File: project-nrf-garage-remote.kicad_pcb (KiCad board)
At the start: 2 copper layers, 9 parts, among them J1 Screw_Terminal_01x02, J2 Screw_Terminal_01x04, Q1 BSS138W, Q2 BSS138W

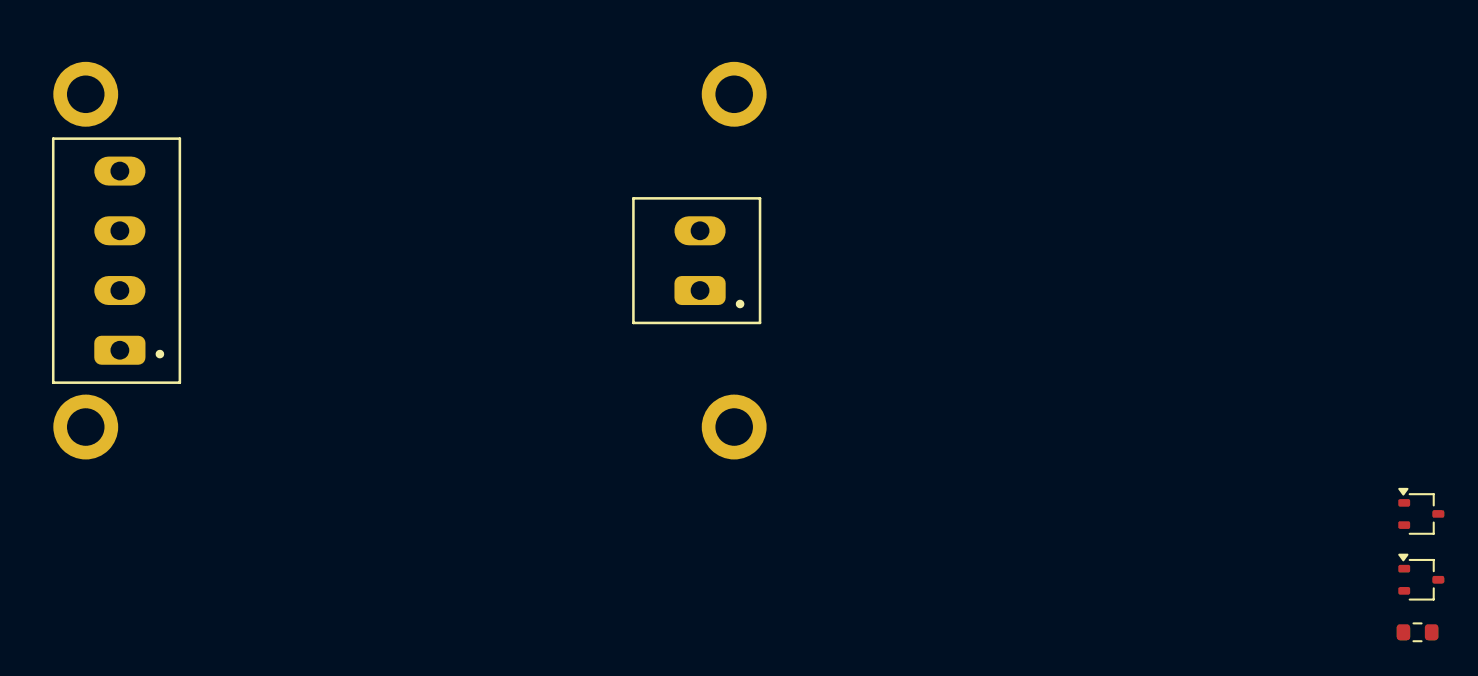
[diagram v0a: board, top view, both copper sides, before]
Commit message: Change the terminals footprint
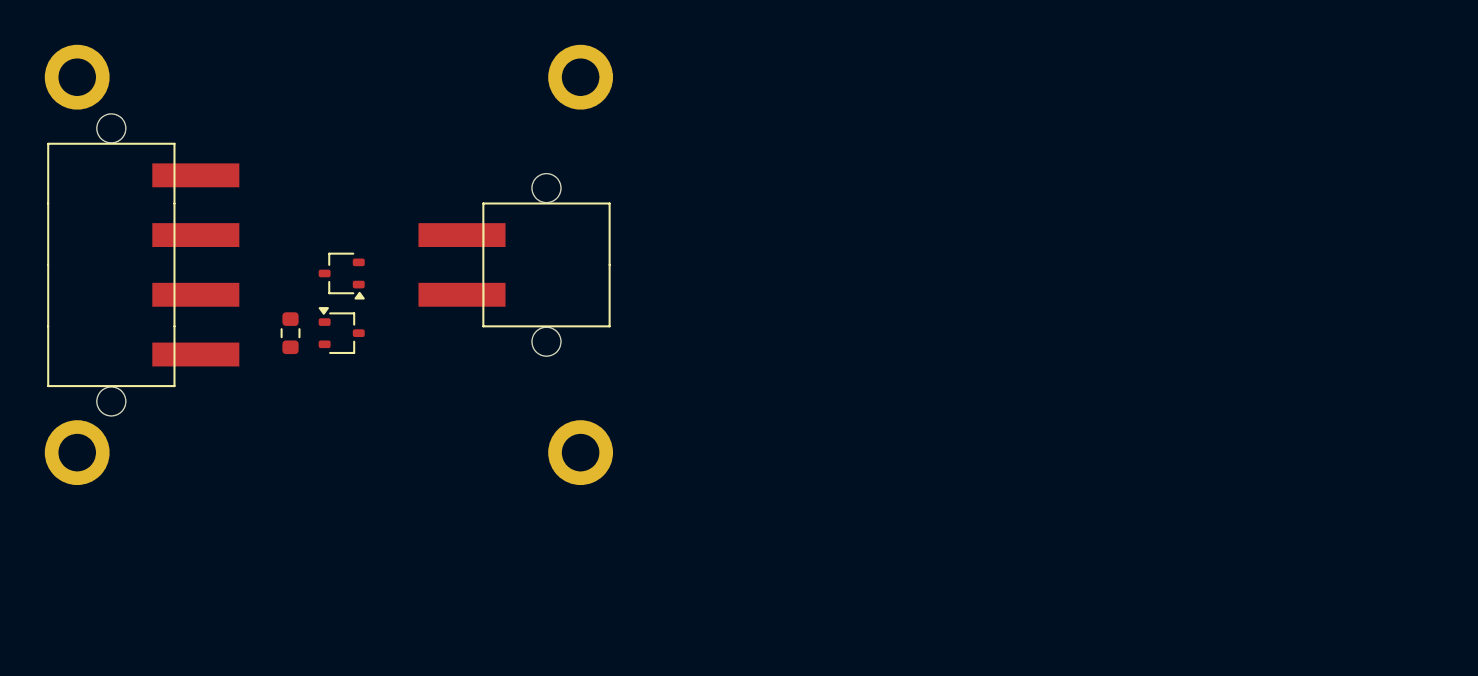
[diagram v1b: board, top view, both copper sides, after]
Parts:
- J1: footprint Conn_Molex_393570002:Molex-393570002-MFG -> TZ022101B000G:TZ022101B000G
- J2: footprint Conn_Molex_393570004:Molex-393570004-MFG -> TZ042101B000G:TZ042101B000G
- moved R1 68.3 mm to (36.0, 32.0), turned to -90 degrees
- moved Q2 65.8 mm to (39.0, 28.5), turned to 180 degrees
- moved Q1 64.1 mm to (39.0, 32.0)
- moved H4 9.12 mm to (53.0, 39.0)
- moved H3 9.06 mm to (53.0, 17.0)
- moved J1 8.81 mm to (51.0, 28.0)
- moved H2 1.58 mm to (23.5, 39.0)
- moved H1 1.12 mm to (23.5, 17.0)
- moved J2 0.39 mm to (25.5, 28.0), turned to -90 degrees

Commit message: Place parts
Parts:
- moved R1 9.34 mm to (38.5, 23.0), turned to 0 degrees
- moved Q1 6.52 mm to (38.5, 25.5)
- moved Q2 1.58 mm to (38.5, 30.0)
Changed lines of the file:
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@@
 	(footprint "BSS138W:BSS138W"
 		(layer "F.Cu")
-		(at 39 32)
+		(at 38.5 25.5)
 		(descr "SOT-323, SC-70")
 		(tags "SOT-323 SC-70")
@@
 	(footprint "BSS138W:BSS138W"
 		(layer "F.Cu")
-		(at 39 28.5 180)
+		(at 38.5 30 180)
 		(descr "SOT-323, SC-70")
 		(tags "SOT-323 SC-70")
@@
 	(footprint "Resistor_SMD:R_0603_1608Metric"
 		(layer "F.Cu")
-		(at 36 32 -90)
+		(at 38.5 23)
 		(descr "Resistor SMD 0603 (1608 Metric), square (rectangular) end terminal, IPC_7351 nominal, (Body size source: IPC-SM-782 page 72, https://www.pcb-3d.com/wordpress/wp-content/uploads/ipc-sm-782a_amendment_1_and_2.pdf), generated with kicad-footprint-generator")
 		(tags "resistor")
 		(property "Reference" "R1"
-			(at 0 -1.43 90)
+			(at 0 -1.43 360)
 			(layer "F.SilkS")
 			(hide yes)
@@
 		)
 		(property "Value" "PD"
-			(at 0 1.43 90)
+			(at 0 1.43 360)
 			(layer "F.Fab")
 			(hide yes)
@@
 		)
 		(property "Footprint" "Resistor_SMD:R_0603_1608Metric"
-			(at 0 0 -90)
+			(at 0 0 0)
 			(unlocked yes)
 			(layer "F.Fab")
@@
 		)
 		(property "Datasheet" ""
-			(at 0 0 -90)
+			(at 0 0 0)
 			(unlocked yes)
 			(layer "F.Fab")
@@
 		)
 		(property "Description" "Resistor"
-			(at 0 0 -90)
+			(at 0 0 0)
 			(unlocked yes)
 			(layer "F.Fab")
@@
 		(attr smd)
 		(fp_line
+			(start -0.237258 -0.5225)
+			(end 0.237258 -0.5225)
+			(stroke
+				(width 0.12)
+				(type solid)
+			)
+			(layer "F.SilkS")
+		)
+		(fp_line
 			(start -0.237258 0.5225)
 			(end 0.237258 0.5225)
@@
 		)
 		(fp_line
-			(start -0.237258 -0.5225)
-			(end 0.237258 -0.5225)
-			(stroke
-				(width 0.12)
-				(type solid)
-			)
-			(layer "F.SilkS")
+			(start -1.48 -0.73)
+			(end 1.48 -0.73)
+			(stroke
+				(width 0.05)
+				(type solid)
+			)
+			(layer "F.CrtYd")
 		)
 		(fp_line
@@
 		)
 		(fp_line
+			(start 1.48 -0.73)
+			(end 1.48 0.73)
+			(stroke
+				(width 0.05)
+				(type solid)
+			)
+			(layer "F.CrtYd")
+		)
+		(fp_line
 			(start 1.48 0.73)
 			(end -1.48 0.73)
@@
 		)
 		(fp_line
-			(start -1.48 -0.73)
-			(end 1.48 -0.73)
-			(stroke
-				(width 0.05)
-				(type solid)
-			)
-			(layer "F.CrtYd")
-		)
-		(fp_line
-			(start 1.48 -0.73)
-			(end 1.48 0.73)
-			(stroke
-				(width 0.05)
-				(type solid)
-			)
-			(layer "F.CrtYd")
+			(start -0.8 -0.4125)
+			(end 0.8 -0.4125)
+			(stroke
+				(width 0.1)
+				(type solid)
+			)
+			(layer "F.Fab")
 		)
 		(fp_line
@@
 		)
 		(fp_line
+			(start 0.8 -0.4125)
+			(end 0.8 0.4125)
+			(stroke
+				(width 0.1)
+				(type solid)
+			)
+			(layer "F.Fab")
+		)
+		(fp_line
 			(start 0.8 0.4125)
 			(end -0.8 0.4125)
@@
 			(layer "F.Fab")
 		)
-		(fp_line
-			(start -0.8 -0.4125)
-			(end 0.8 -0.4125)
-			(stroke
-				(width 0.1)
-				(type solid)
-			)
-			(layer "F.Fab")
-		)
-		(fp_line
-			(start 0.8 -0.4125)
-			(end 0.8 0.4125)
-			(stroke
-				(width 0.1)
-				(type solid)
-			)
-			(layer "F.Fab")
-		)
 		(fp_text user "${REFERENCE}"
-			(at 0 0 90)
+			(at 0 0 360)
 			(layer "F.Fab")
 			(effects
@@
 		)
 		(pad "1" smd roundrect
-			(at -0.825 0 270)
+			(at -0.825 0)
 			(size 0.8 0.95)
 			(layers "F.Cu" "F.Paste" "F.Mask")
@@
 		)
 		(pad "2" smd roundrect
-			(at 0.825 0 270)
+			(at 0.825 0)
 			(size 0.8 0.95)
 			(layers "F.Cu" "F.Paste" "F.Mask")

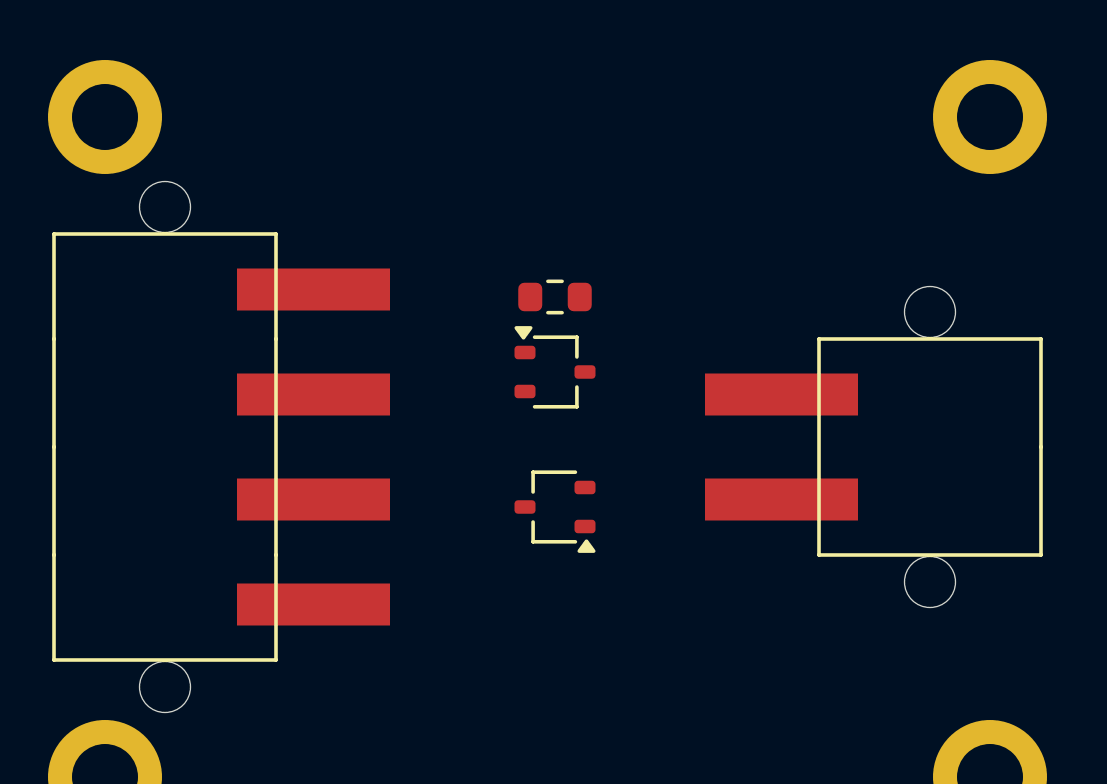
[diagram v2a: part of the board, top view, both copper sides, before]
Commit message: Add silkscreen
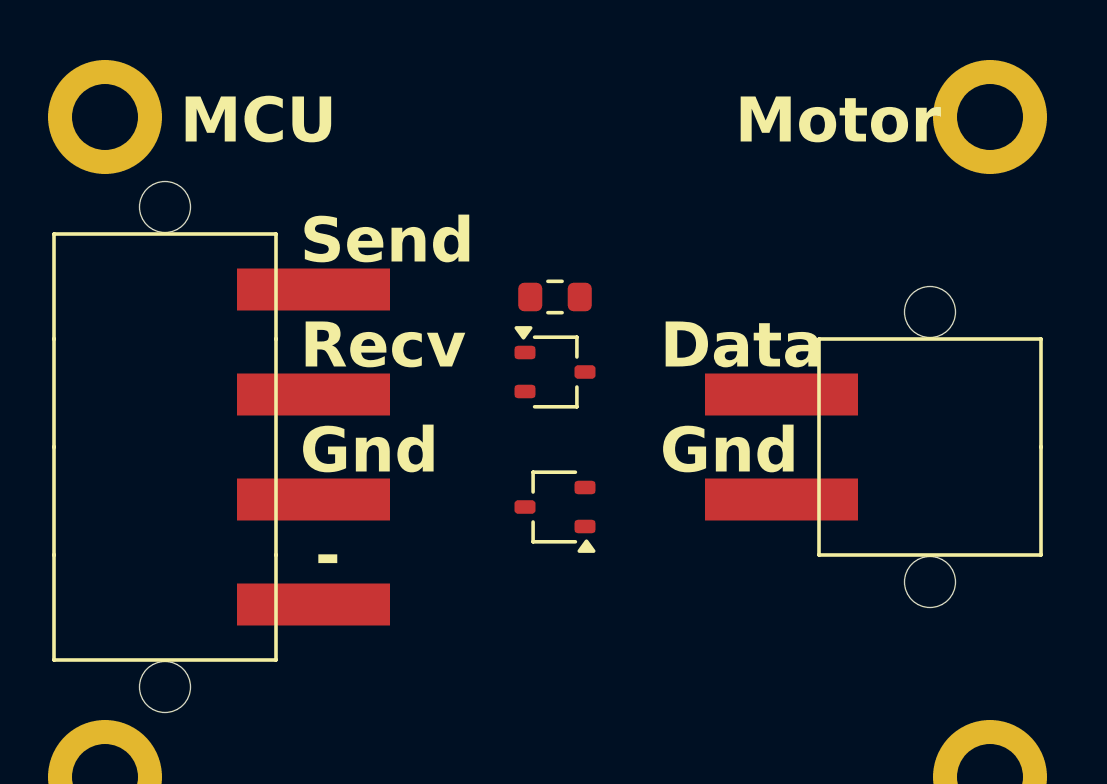
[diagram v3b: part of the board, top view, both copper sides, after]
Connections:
- J1 pad 1: /motor_data -> GND
- J1 pad 2: GND -> /motor_data
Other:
- board text added: "-"
- board text added: "Data"
- board text added: "François Gervais 15 oct. 2024 v1.0.0"
- board text added: "Gnd"
- board text added: "MCU"
- board text added: "Motor"
- board text added: "Recv"
- board text added: "Send"

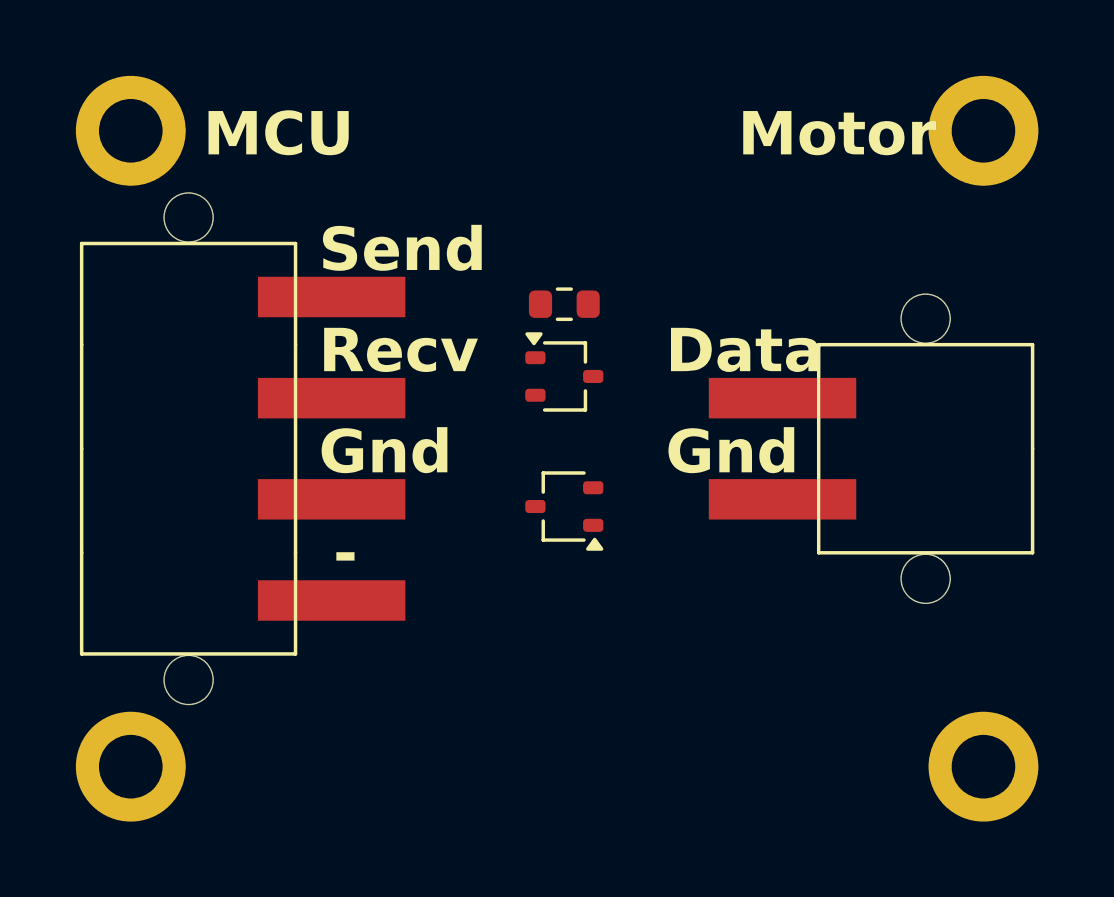
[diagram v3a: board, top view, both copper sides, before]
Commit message: Add board outline
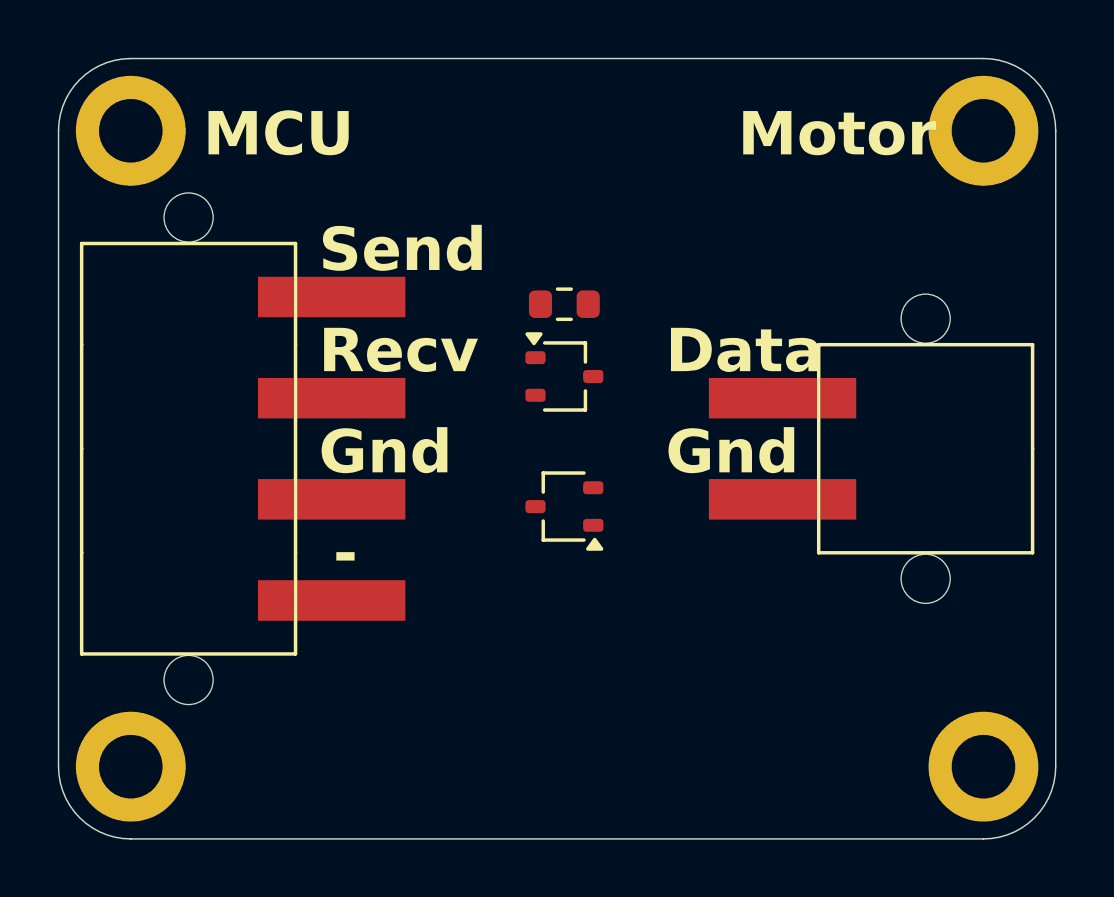
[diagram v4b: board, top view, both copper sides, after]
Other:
- board outline added: 34.5 x 27 mm
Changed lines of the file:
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@@
 		)
+	)
+	(gr_line
+		(start 53 41.5)
+		(end 23.5 41.5)
+		(stroke
+			(width 0.05)
+			(type default)
+		)
+		(layer "Edge.Cuts")
+	)
+	(gr_line
+		(start 23.5 14.5)
+		(end 53 14.5)
+		(stroke
+			(width 0.05)
+			(type default)
+		)
+		(layer "Edge.Cuts")
+	)
+	(gr_line
+		(start 55.5 17)
+		(end 55.5 39)
+		(stroke
+			(width 0.05)
+			(type default)
+		)
+		(layer "Edge.Cuts")
+	)
+	(gr_arc
+		(start 53 14.5)
+		(mid 54.767767 15.232233)
+		(end 55.5 17)
+		(stroke
+			(width 0.05)
+			(type default)
+		)
+		(layer "Edge.Cuts")
+	)
+	(gr_arc
+		(start 21 17)
+		(mid 21.732233 15.232233)
+		(end 23.5 14.5)
+		(stroke
+			(width 0.05)
+			(type default)
+		)
+		(layer "Edge.Cuts")
+	)
+	(gr_line
+		(start 21 39)
+		(end 21 17)
+		(stroke
+			(width 0.05)
+			(type default)
+		)
+		(layer "Edge.Cuts")
+	)
+	(gr_arc
+		(start 23.5 41.5)
+		(mid 21.732233 40.767767)
+		(end 21 39)
+		(stroke
+			(width 0.05)
+			(type default)
+		)
+		(layer "Edge.Cuts")
+	)
+	(gr_arc
+		(start 55.5 39)
+		(mid 54.767767 40.767767)
+		(end 53 41.5)
+		(stroke
+			(width 0.05)
+			(type default)
+		)
+		(layer "Edge.Cuts")
 	)
 	(gr_text "François Gervais\n15 oct. 2024\nv1.0.0"

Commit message: Add routing
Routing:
- net /motor_data: track 0.00 -> 11.6 mm
- net /uc_send: track 0.00 -> 9.25 mm
- net GND: track 0.00 -> 9.22 mm, vias 0 -> 5
- net /uc_recv: track 0.00 -> 8.60 mm
- added copper zone on B.Cu, net GND
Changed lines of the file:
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@@
+		)
+	)
+	(segment
+		(start 39.5 29.35)
+		(end 39.5 28.5)
+		(width 0.2)
+		(layer "F.Cu")
+		(net 1)
+	)
+	(segment
+		(start 30.45 29.75)
+		(end 33.75 29.75)
+		(width 0.2)
+		(layer "F.Cu")
+		(net 1)
+	)
+	(segment
+		(start 37.5 26.15)
+		(end 37.5 27)
+		(width 0.2)
+		(layer "F.Cu")
+		(net 1)
+	)
+	(segment
+		(start 39.325 23)
+		(end 40.25 23)
+		(width 0.2)
+		(layer "F.Cu")
+		(net 1)
+	)
+	(segment
+		(start 46.05 29.75)
+		(end 42.75 29.75)
+		(width 0.2)
+		(layer "F.Cu")
+		(net 1)
+	)
+	(via
+		(at 39.5 28.5)
+		(size 0.6)
+		(drill 0.3)
+		(layers "F.Cu" "B.Cu")
+		(net 1)
+	)
+	(via
+		(at 40.25 23)
+		(size 0.6)
+		(drill 0.3)
+		(layers "F.Cu" "B.Cu")
+		(net 1)
+	)
+	(via
+		(at 37.5 27)
+		(size 0.6)
+		(drill 0.3)
+		(layers "F.Cu" "B.Cu")
+		(net 1)
+	)
+	(via
+		(at 33.75 29.75)
+		(size 0.6)
+		(drill 0.3)
+		(layers "F.Cu" "B.Cu")
+		(net 1)
+	)
+	(via
+		(at 42.75 29.75)
+		(size 0.6)
+		(drill 0.3)
+		(layers "F.Cu" "B.Cu")
+		(net 1)
+	)
+	(segment
+		(start 46.05 26.25)
+		(end 40.25 26.25)
+		(width 0.2)
+		(layer "F.Cu")
+		(net 2)
+	)
+	(segment
+		(start 39.5 30.65)
+		(end 40.25 29.9)
+		(width 0.2)
+		(layer "F.Cu")
+		(net 2)
+	)
+	(segment
+		(start 40.25 26.25)
+		(end 39.5 25.5)
+		(width 0.2)
+		(layer "F.Cu")
+		(net 2)
+	)
+	(segment
+		(start 40.25 29.9)
+		(end 40.25 26.25)
+		(width 0.2)
+		(layer "F.Cu")
+		(net 2)
+	)
+	(segment
+		(start 37.5 23.175)
+		(end 37.675 23)
+		(width 0.2)
+		(layer "F.Cu")
+		(net 3)
+	)
+	(segment
+		(start 37.425 22.75)
+		(end 37.675 23)
+		(width 0.2)
+		(layer "F.Cu")
+		(net 3)
+	)
+	(segment
+		(start 30.45 22.75)
+		(end 37.425 22.75)
+		(width 0.2)
+		(layer "F.Cu")
+		(net 3)
+	)
+	(segment
+		(start 37.5 24.85)
+		(end 37.5 23.175)
+		(width 0.2)
+		(layer "F.Cu")
+		(net 3)
+	)
+	(segment
+		(start 33.75 26.25)
+		(end 37.5 30)
+		(width 0.2)
+		(layer "F.Cu")
+		(net 5)
+	)
+	(segment
+		(start 30.45 26.25)
+		(end 33.75 26.25)
+		(width 0.2)
+		(layer "F.Cu")
+		(net 5)
+	)
+	(zone
+		(net 1)
+		(net_name "GND")
+		(layer "B.Cu")
+		(hatch edge 0.5)
+		(connect_pads
+			(clearance 0.5)
+		)
+		(min_thickness 0.25)
+		(filled_areas_thickness no)
+		(fill yes
+			(thermal_gap 0.5)
+			(thermal_bridge_width 0.5)
+		)
+		(polygon
+			(pts
+				(xy 21 41.5) (xy 21 14.5) (xy 55.5 14.5) (xy 55.5 41.5)
+			)
 		)
 	)
